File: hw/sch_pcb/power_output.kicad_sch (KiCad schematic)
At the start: 20 parts, among them J12 HEADER_2x05_PARALLEL, J2 CONN1_1, J3 CONN1_1, J4 JUMP_4X2, J5 HEADER_2x03_PARALLEL, U2 LMR14050

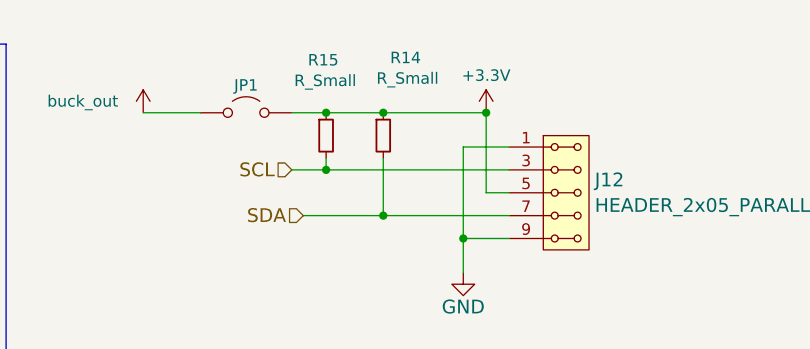
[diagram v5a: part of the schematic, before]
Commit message: Syncing board with schematics. Roughly placing the switching regulator.
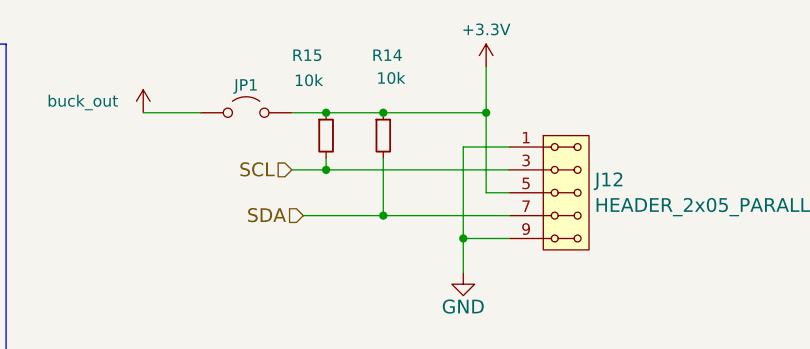
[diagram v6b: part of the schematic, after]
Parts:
- J5: footprint (none) -> Mlab_Pin_Headers:Straight_2x03
- JP1: footprint (none) -> Mlab_Pin_Headers:Straight_2x01
- L2: footprint Inductor_SMD:L_Wuerth_HCI-1050 -> Inductor_SMD:L_Vishay_IHLP-2020; UST_ID 6087af42128750769ee59060 -> 669e8efe6fdfe6f54e2eb7e6
- R14, R15: value R_Small -> 10k; footprint (none) -> Resistor_SMD:R_0805_2012Metric
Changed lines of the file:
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@@
+	(wire
+		(pts
+			(xy 243.84 21.59) (xy 243.84 26.67)
+		)
+		(stroke
+			(width 0)
+			(type default)
+		)
+	)
 	(wire
 		(pts
@@
 		(dnp no)
 		(property "Reference" "R15"
-			(at 224.028 20.828 0)
+			(at 222.25 20.32 0)
 			(effects
 				(font
@@
 			)
 		)
-		(property "Value" "R_Small"
+		(property "Value" "10k"
 			(at 222.504 23.114 0)
 			(effects
@@
 			)
 		)
-		(property "Footprint" ""
+		(property "Footprint" "Resistor_SMD:R_0805_2012Metric"
 			(at 226.06 29.21 0)
 			(effects
@@
 		)
 		(property "Description" "Resistor, small symbol"
+			(at 226.06 29.21 0)
+			(effects
+				(font
+					(size 1.27 1.27)
+				)
+				(hide yes)
+			)
+		)
+		(property "UST_ID" ""
 			(at 226.06 29.21 0)
 			(effects
@@
 			)
 		)
-		(property "Footprint" ""
+		(property "Footprint" "Mlab_Pin_Headers:Straight_2x03"
 			(at 252.73 58.42 0)
 			(effects
@@
 					(size 1.524 1.524)
 				)
+				(hide yes)
 			)
 		)
@@
 	(symbol
 		(lib_id "power:+3.3V")
-		(at 243.84 26.67 0)
+		(at 243.84 21.59 0)
 		(unit 1)
 		(exclude_from_sim no)
@@
 		(fields_autoplaced yes)
 		(property "Reference" "#PWR02"
-			(at 243.84 30.48 0)
+			(at 243.84 25.4 0)
 			(effects
 				(font
@@
 		)
 		(property "Value" "+3.3V"
-			(at 243.84 22.5369 0)
+			(at 243.84 17.4569 0)
 			(effects
 				(font
@@
 		)
 		(property "Footprint" ""
-			(at 243.84 26.67 0)
+			(at 243.84 21.59 0)
 			(effects
 				(font
@@
 		)
 		(property "Datasheet" ""
-			(at 243.84 26.67 0)
+			(at 243.84 21.59 0)
 			(effects
 				(font
@@
 		)
 		(property "Description" "Power symbol creates a global label with name \"+3.3V\""
-			(at 243.84 26.67 0)
+			(at 243.84 21.59 0)
 			(effects
 				(font
@@
 			)
 		)
-		(property "Footprint" "Inductor_SMD:L_Wuerth_HCI-1050"
+		(property "Footprint" "Inductor_SMD:L_Vishay_IHLP-2020"
 			(at 156.21 102.87 0)
 			(effects
@@
 			)
 		)
-		(property "Datasheet" "~"
+		(property "Datasheet" "https://www.vishay.com/docs/34563/ihlp-2020cz-8a.pdf"
 			(at 156.21 102.87 0)
 			(effects
@@
 			)
 		)
-		(property "UST_ID" "6087af42128750769ee59060"
+		(property "UST_ID" "669e8efe6fdfe6f54e2eb7e6"
 			(at 156.21 102.87 0)
 			(effects
@@
 			)
 		)
-		(property "Footprint" ""
+		(property "Footprint" "Mlab_Pin_Headers:Straight_2x01"
 			(at 217.17 26.67 0)
 			(effects
@@
 		(dnp no)
 		(property "Reference" "R14"
-			(at 233.172 20.574 0)
+			(at 231.14 20.32 0)
 			(effects
 				(font
@@
 			)
 		)
-		(property "Value" "R_Small"
+		(property "Value" "10k"
 			(at 231.648 22.86 0)
 			(effects
@@
 			)
 		)
-		(property "Footprint" ""
+		(property "Footprint" "Resistor_SMD:R_0805_2012Metric"
 			(at 232.41 29.21 0)
 			(effects
@@
 			(at 232.41 29.21 0)
 			(effects
+				(font
+					(size 1.27 1.27)
+				)
+				(hide yes)
+			)
+		)
+		(property "UST_ID" ""
+			(at 232.41 29.21 0)
+			(effects

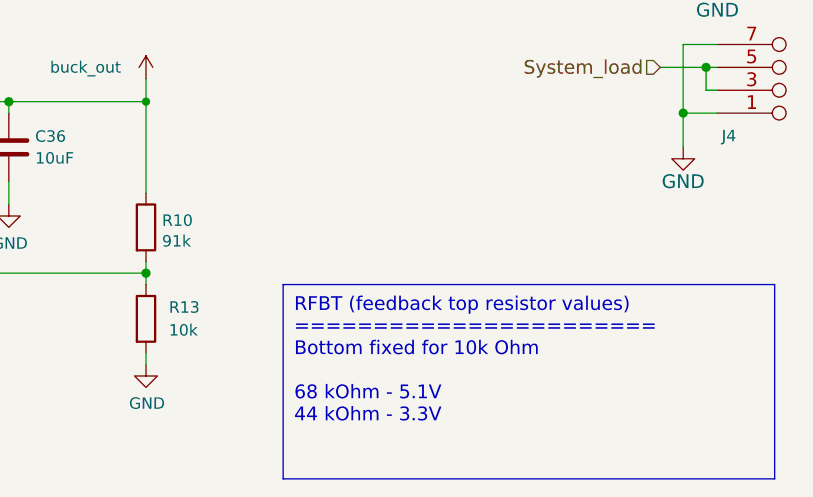
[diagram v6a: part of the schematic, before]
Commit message: Routed switching regulator Starting of layout cleanup. Uniforming of charger and switching regulator inductors.
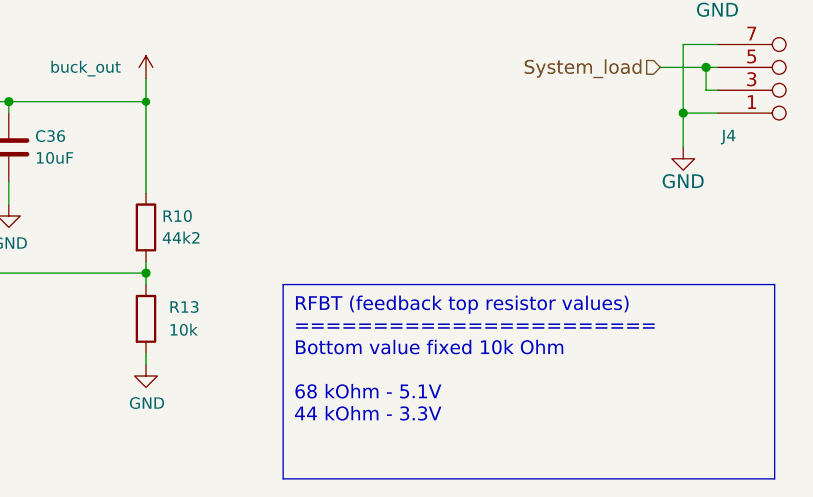
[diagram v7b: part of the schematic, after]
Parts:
- R10: value 91k -> 44k2; UST_ID 5c70984712875079b91f8a95 -> 669ebdcc6fdfe6f54e2eb869
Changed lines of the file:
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@@
 		)
 	)
-	(text_box "RFBT (feedback top resistor values)\n=======================\nBottom fixed for 10k Ohm\n\n68 kOhm - 5.1V\n44 kOhm - 3.3V"
+	(text_box "RFBT (feedback top resistor values)\n=======================\nBottom value fixed 10k Ohm\n\n68 kOhm - 5.1V\n44 kOhm - 3.3V"
 		(exclude_from_sim no)
 		(at 208.28 123.19 0)
@@
 		)
 	)
+	(netclass_flag ""
+		(length 2.54)
+		(shape round)
+		(at 146.05 96.52 270)
+		(fields_autoplaced yes)
+		(effects
+			(font
+				(size 1.524 1.524)
+			)
+			(justify right bottom)
+		)
+		(property "Netclass" "HIGH_I"
+			(at 148.59 95.5548 90)
+			(effects
+				(font
+					(size 1.27 1.27)
+					(italic yes)
+				)
+				(justify left)
+			)
+		)
+	)
+	(netclass_flag ""
+		(length 2.54)
+		(shape round)
+		(at 167.64 102.87 0)
+		(fields_autoplaced yes)
+		(effects
+			(font
+				(size 1.524 1.524)
+			)
+			(justify left bottom)
+		)
+		(property "Netclass" "HIGH_I"
+			(at 168.6052 100.33 0)
+			(effects
+				(font
+					(size 1.27 1.27)
+					(italic yes)
+				)
+				(justify left)
+			)
+		)
+	)
 	(symbol
 		(lib_id "LION2CELL01D-rescue:JUMP_4X2")
@@
 		(fields_autoplaced yes)
 		(property "Reference" "R10"
-			(at 194.8181 116.0791 0)
-			(effects
-				(font
-					(size 1.27 1.27)
-				)
-				(justify left)
-			)
-		)
-		(property "Value" "91k"
-			(at 194.8181 118.3778 0)
+			(at 194.818 115.6278 0)
+			(effects
+				(font
+					(size 1.27 1.27)
+				)
+				(justify left)
+			)
+		)
+		(property "Value" "44k2"
+			(at 194.818 118.0521 0)
 			(effects
 				(font
@@
 			)
 		)
-		(property "UST_ID" "5c70984712875079b91f8a95"
+		(property "UST_ID" "669ebdcc6fdfe6f54e2eb869"
 			(at 193.04 116.84 0)
 			(effects
